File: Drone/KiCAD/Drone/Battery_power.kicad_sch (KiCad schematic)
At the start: 7 parts, among them U4 LD1117S25TR_SOT223, U5 LD1117S25TR_SOT223

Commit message: Added sheet formalities
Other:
- title: (none) -> Lightweight drone - Power Distribution
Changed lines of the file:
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@@
 (kicad_sch (version 20230121) (generator eeschema)
   (paper "A4")
+  (title_block
+    (title "Lightweight drone - Power Distribution")
+    (date "2024-09-29")
+    (rev "V1")
+  )
   (junction (at 58.42 48.26) (diameter 0) (color 0 0 0 0)
   )

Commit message: MOSFET driver consideration
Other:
- note added: "Alternatively, use ferrite beads for VDDA. But what frequencies need attenuation? (All SPI @ 10Mhz, DC-Motor control PWM frequency 20kHz)"
- note added: "To debug, connect power supply to battery plug (include extra plug in BOM)."
- note removed: "Alternatively, use ferrite beads for VDDA. But what frequencies need attenuation? (All SPI @ 10Mhz, DC-Motor control PWM frequency ??)"
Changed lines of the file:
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@@
     (stroke (width 0) (type default))
   )
-  (text "Alternatively, use ferrite beads for VDDA. \nBut what frequencies need attenuation?\n(All SPI @ 10Mhz, DC-Motor control PWM frequency ??)"
+  (text "To debug, connect power supply\nto battery plug (include extra \nplug in BOM)."
+    (at 17.78 69.85 0)
+    (effects (font (size 1.27 1.27)) (justify left bottom))
+  )
+  (text "Alternatively, use ferrite beads for VDDA. \nBut what frequencies need attenuation?\n(All SPI @ 10Mhz, DC-Motor control PWM frequency 20kHz)"
     (at 123.19 62.23 0)
     (effects (font (size 1.27 1.27)) (justify left bottom))

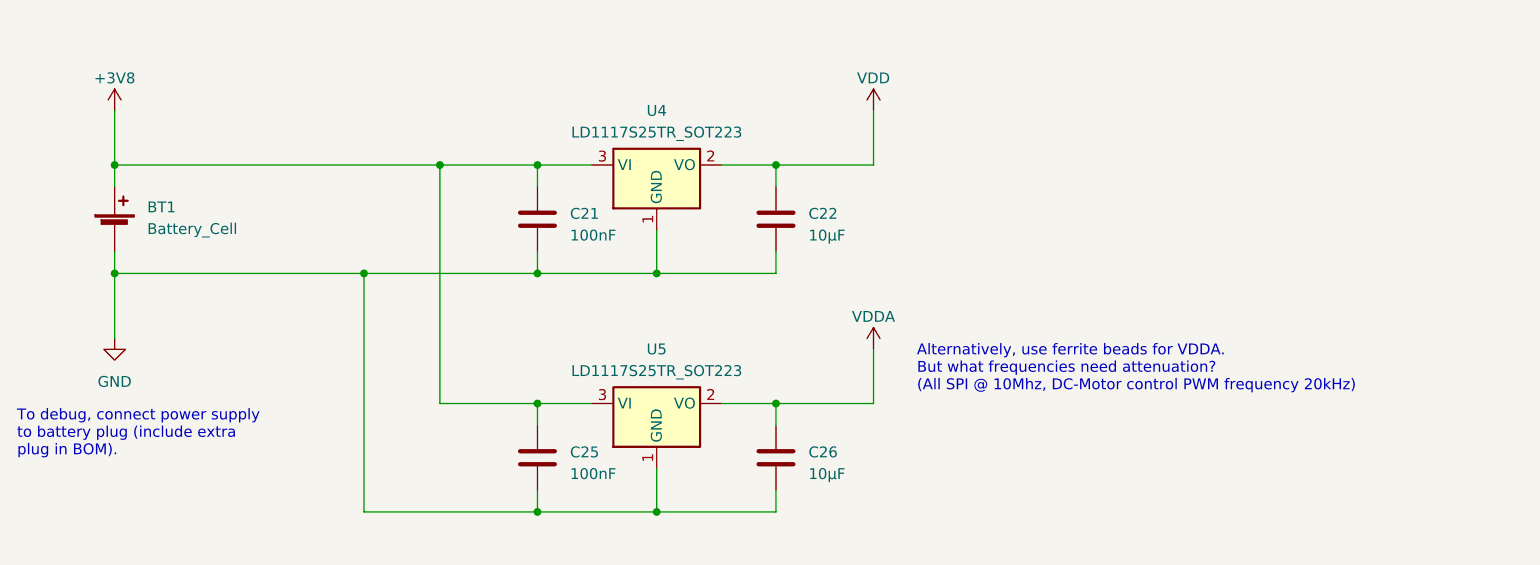
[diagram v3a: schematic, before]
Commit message: new LDO, programming and µC connections
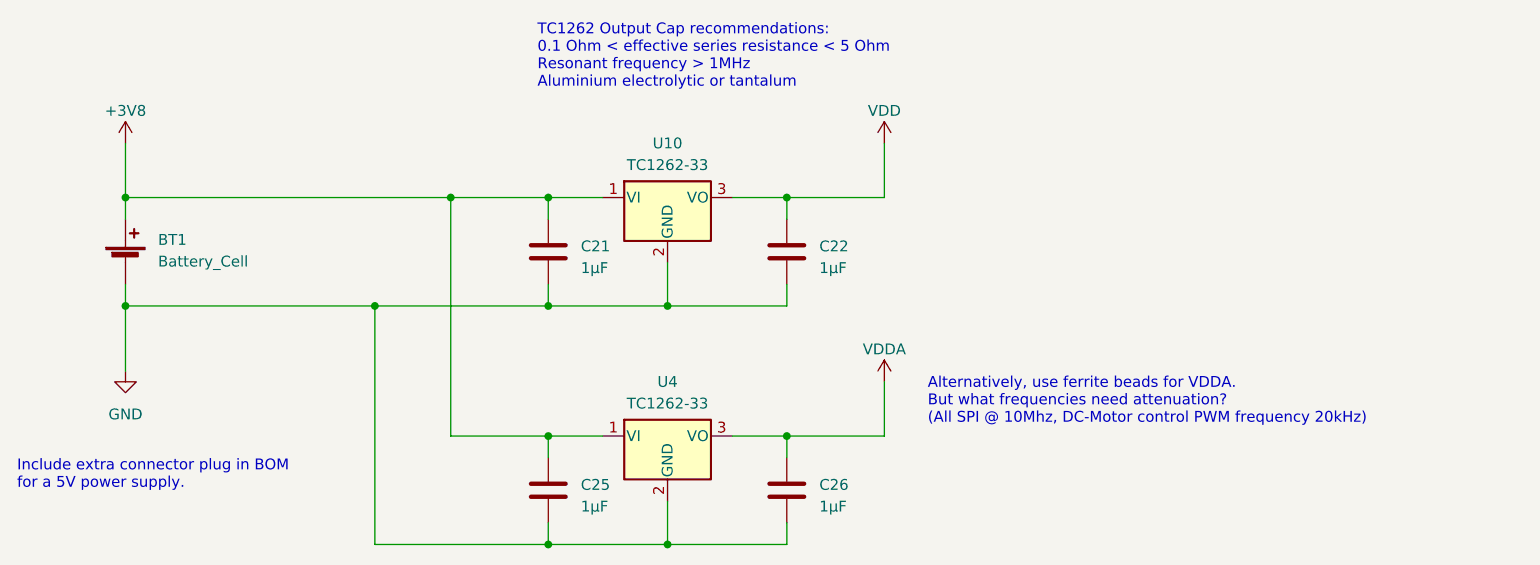
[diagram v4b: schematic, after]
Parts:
- removed U4, U5: LD1117S25TR_SOT223, Package_TO_SOT_SMD:SOT-223-3_TabPin2, symbol Regulator_Linear:LD1117S25TR_SOT223
- added U10, U4: TC1262-33, symbol Regulator_Linear:TC1262-33
- C21, C25: value 100nF -> 1µF
- C22, C26: value 10µF -> 1µF
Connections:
- net +3V8: now also U10.1 (VI), U4.1 (VI)
- net GND: now also U10.2 (GND), U4.2 (GND)
- net VDD: now also U10.3 (VO)
- net VDDA: now also U4.3 (VO)
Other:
- note added: "Include extra connector plug in BOM for a 5V power supply."
- note added: "TC1262 Output Cap recommendations: 0.1 Ohm < effective series resistance < 5 Ohm Resonant frequency > 1MHz Aluminium electrolytic or tantalum"
- note removed: "To debug, connect power supply to battery plug (include extra plug in BOM)."
- moved on the sheet: BT1, C21, C22, C25, C26
